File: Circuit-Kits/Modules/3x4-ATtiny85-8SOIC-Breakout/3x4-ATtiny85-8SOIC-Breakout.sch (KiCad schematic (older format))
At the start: 0 parts

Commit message: Add 3x4 555 Timer and 3x4 ATtiny85 schematic.
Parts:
- added U1: ATTINY85-8SOIC, symbol ATTINY85-P
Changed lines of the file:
@@
 Title "3x4 ATtiny85 8SOIC Breakout Module"
 Date "17 Mar 2017"
-Rev"1.0"
-Comp "All rights reserved.")
-Comment1 "help@browndoggadgets.com")
-Comment2 "http://browndoggadgets.com/")
-Comment3 "Brown Dog Gadgets")
+Rev "1.0"
+Comp "All rights reserved."
+Comment1 "help@browndoggadgets.com"
+Comment2 "http://browndoggadgets.com/"
+Comment3 "Brown Dog Gadgets"
 Comment4 ""
 $EndDescr
+$Comp
+L ATTINY85-P U1
+U 1 1 5880402D
+P 5025 3975
+F 0 "U1" H 3875 4375 50  0000 C CNN
+F 1 "ATTINY85-8SOIC" H 5925 3575 50  0000 C CNN
+F 2 "" H 6025 3975 50  0000 C CIN
+F 3 "" H 5025 3975 50  0000 C CNN
+F 4 "IC MCU 8BIT ATTINY85 8SOIC" H 5025 3975 60  0001 C CNN "Description"
+F 5 "Microchip" H 5025 3975 60  0001 C CNN "MF_Name"
+F 6 "ATTINY85-20SU" H 5025 3975 60  0001 C CNN "MF_PN"
+F 7 "Digikey" H 5025 3975 60  0001 C CNN "S1_Name"
+F 8 "ATTINY85-20SU-ND" H 5025 3975 60  0001 C CNN "S1_PN"
+	1    5025 3975
+	1    0    0    -1
+$EndComp
 $EndSCHEMATC

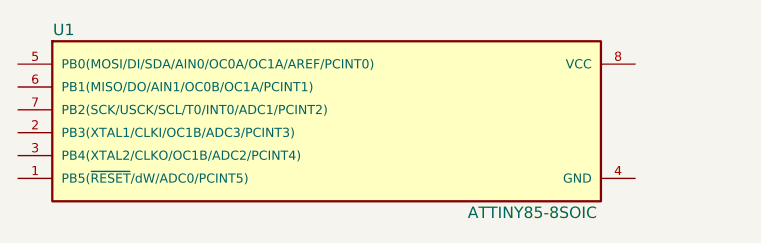
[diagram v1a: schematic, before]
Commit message: Add 3x4 ATtiny85 v1.0
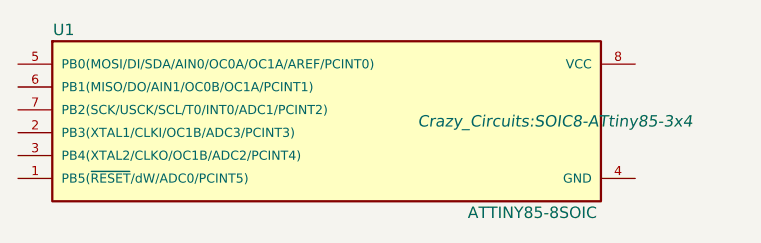
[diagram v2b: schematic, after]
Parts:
- U1: footprint (none) -> Crazy_Circuits:SOIC8-ATtiny85-3x4
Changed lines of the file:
@@
 EESchema Schematic File Version 2
 LIBS:crazy_circuits
+LIBS:3x4-ATtiny85-8SOIC-Breakout-cache
 EELAYER 25 0
 EELAYER END
@@
 F 0 "U1" H 3875 4375 50  0000 C CNN
 F 1 "ATTINY85-8SOIC" H 5925 3575 50  0000 C CNN
-F 2 "" H 6025 3975 50  0000 C CIN
+F 2 "Crazy_Circuits:SOIC8-ATtiny85-3x4" H 6025 3975 50  0000 C CIN
 F 3 "" H 5025 3975 50  0000 C CNN
 F 4 "IC MCU 8BIT ATTINY85 8SOIC" H 5025 3975 60  0001 C CNN "Description"
